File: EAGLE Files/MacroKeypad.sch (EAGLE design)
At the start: 8 parts

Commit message: Clean up old files
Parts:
- removed S2: (no value), switch:255SB
- removed U$6: CHERRY-MX, cherrymx:CHERRY-MX
- added S1: MOMENTARY-SWITCH-SPST-PTH-6.0MM, SparkFun-Switches:MOMENTARY-SWITCH-SPST-PTH-6.0MM
- added U$7: CHERRY-MX-LED, cherrymx:CHERRY-MX-LED
- U$1, U$2, U$3, U$4, U$5: value CHERRY-MX -> CHERRY-MX-LED; device cherrymx:CHERRY-MX -> cherrymx:CHERRY-MX-LED
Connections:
- new net LED+: B1.A3, B1.VCC, U$1.LED+, U$2.LED+, U$3.LED+, U$4.LED+, U$5.LED+, U$7.LED+
- net GND: now also S1.1, U$1.LED-, U$1.SW2, U$2.LED-, U$2.SW2, U$3.LED-, U$3.SW2, U$4.LED-, U$4.SW2, U$5.LED-, U$5.SW2, U$7.LED-, U$7.SW2; no longer S2.O, U$1.PIN-2, U$2.PIN-2, U$3.PIN-2, U$4.PIN-2, U$5.PIN-2, U$6.PIN-2
- net RESET: now also S1.2; no longer S2.P
- net SW1: now also U$7.SW1; no longer U$1.PIN-1
- net SW2: now also U$3.SW1; no longer U$2.PIN-1
- net SW3: now also U$4.SW1; no longer U$3.PIN-1
- net SW4: now also U$1.SW1; no longer U$4.PIN-1
- net SW5: now also U$2.SW1; no longer U$5.PIN-1
- net SW6: now also U$5.SW1; no longer U$6.PIN-1

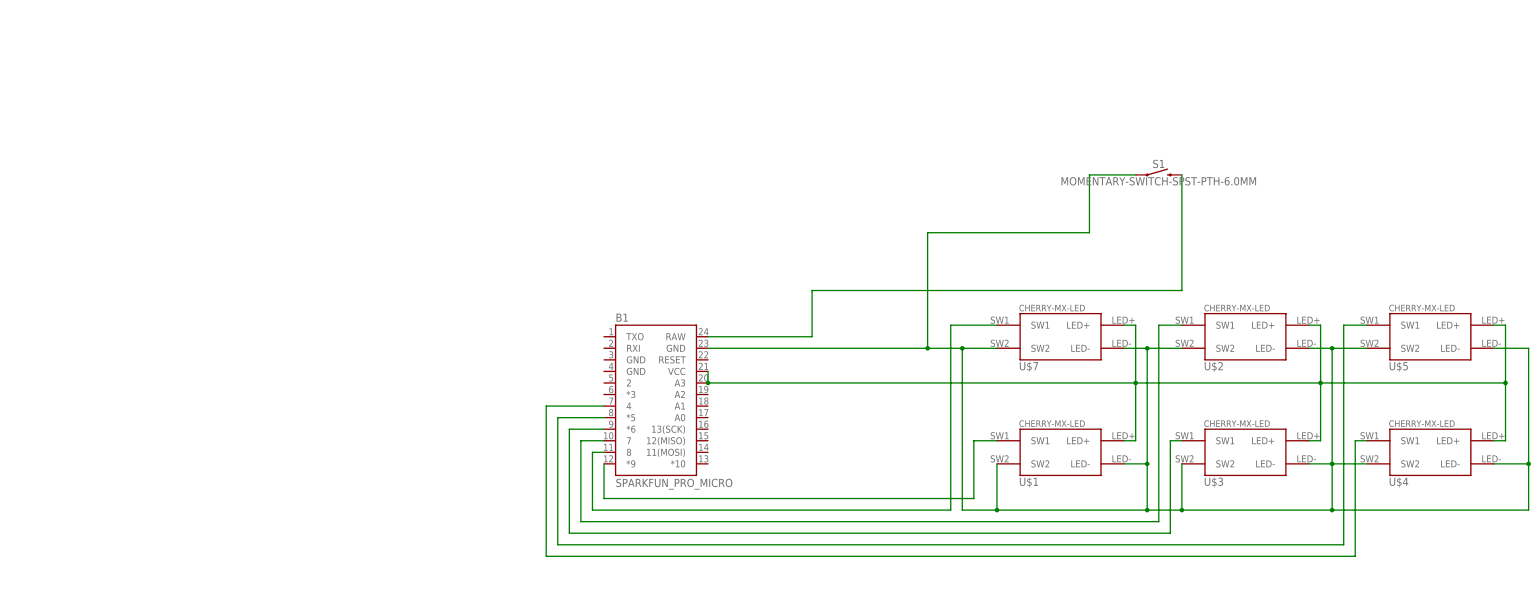
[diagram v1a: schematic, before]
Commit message: Brand new PCB started
Started redesigning PCB and added BOM
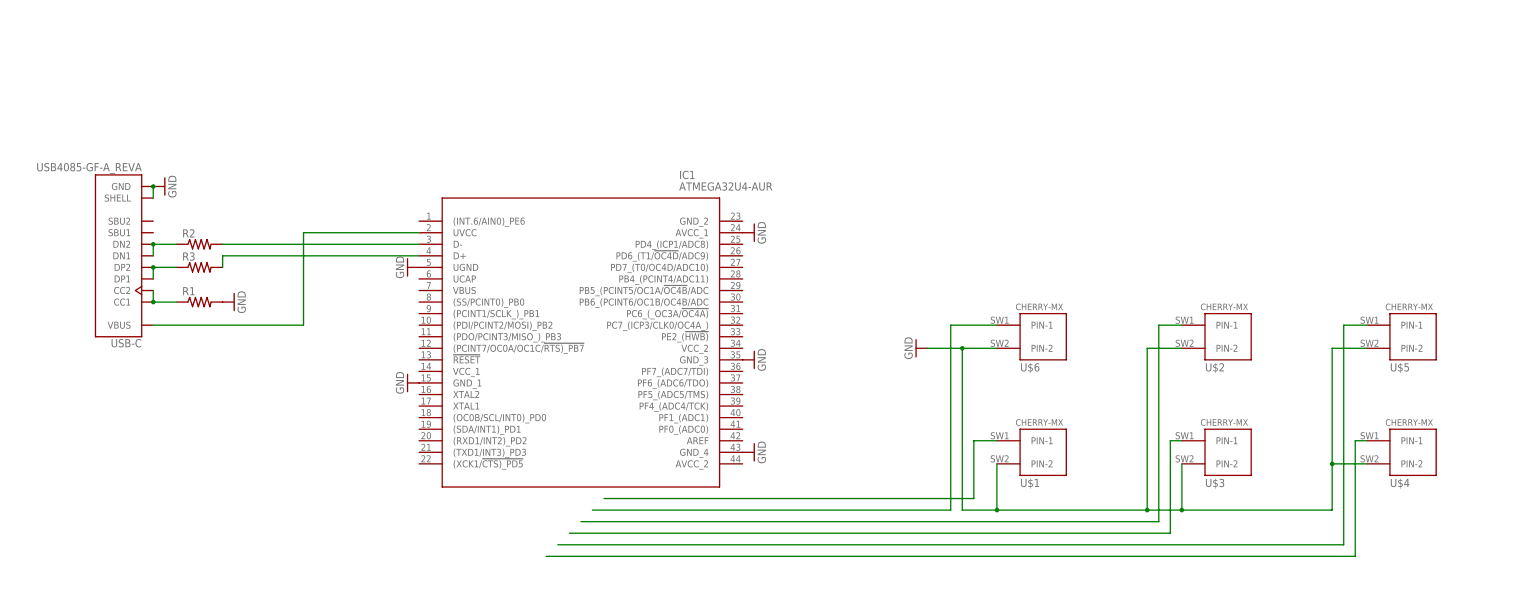
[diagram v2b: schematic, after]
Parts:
- removed B1: SPARKFUN_PRO_MICRO, SparkFun-Boards:SPARKFUN_PRO_MICRO
- removed S1: MOMENTARY-SWITCH-SPST-PTH-6.0MM, SparkFun-Switches:MOMENTARY-SWITCH-SPST-PTH-6.0MM
- removed U$7: CHERRY-MX-LED, cherrymx:CHERRY-MX-LED
- added IC1: ATMEGA32U4-AUR, SamacSys_Parts:ATMEGA32U4-AUR
- added R1: (no value), adafruit:R-US_R0603
- added R2, R3: (no value), adafruit:R-US_R0805
- added U$6: CHERRY-MX, cherrymx:CHERRY-MX
- added USB-C: USB4085-GF-A_REVA, USB4085-GF-A_REVA:USB4085-GF-A_REVA
- U$1, U$2, U$3, U$4, U$5: value CHERRY-MX-LED -> CHERRY-MX; device cherrymx:CHERRY-MX-LED -> cherrymx:CHERRY-MX
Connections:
- removed net LED+: B1.A3, B1.VCC, U$1.LED+, U$2.LED+, U$3.LED+, U$4.LED+, U$5.LED+, U$7.LED+
- removed net RESET: B1.RAW, S1.2
- new net N$1: R1.1, USB-C.CC1, USB-C.CC2
- new net N$2: IC1.UVCC, USB-C.VBUS
- new net N$3: R3.1, USB-C.DP1, USB-C.DP2
- new net N$4: R2.1, USB-C.DN1, USB-C.DN2
- new net N$5: IC1.D-, R2.2
- new net N$6: IC1.D+, R3.2
- net GND: now also IC1.AVCC_1, IC1.GND_1, IC1.GND_3, IC1.GND_4, IC1.UGND, R1.2, U$1.PIN-2, U$2.PIN-2, U$3.PIN-2, U$4.PIN-2, U$5.PIN-2, U$6.PIN-2, USB-C.GND, USB-C.SHELL; no longer B1.GND@2, S1.1, U$1.LED-, U$1.SW2, U$2.LED-, U$2.SW2, U$3.LED-, U$3.SW2, U$4.LED-, U$4.SW2, U$5.LED-, U$5.SW2, U$7.LED-, U$7.SW2
- net SW1: now also U$6.PIN-1; no longer B1.8, U$7.SW1
- net SW2: now also U$3.PIN-1; no longer B1.*6, U$3.SW1
- net SW3: now also U$4.PIN-1; no longer B1.4, U$4.SW1
- net SW4: now also U$1.PIN-1; no longer B1.*9, U$1.SW1
- net SW5: now also U$2.PIN-1; no longer B1.7, U$2.SW1
- net SW6: now also U$5.PIN-1; no longer B1.*5, U$5.SW1

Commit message: Update more files
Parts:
- removed IC1: ATMEGA32U4-AUR, SamacSys_Parts:ATMEGA32U4-AUR
- removed U$1, U$2, U$3, U$4, U$5: CHERRY-MX, cherrymx:CHERRY-MX
- added C1: 1uF, adafruit:C-USC0805
- added IC2: ATMEGA32U4-MU, SamacSys_Parts:ATMEGA32U4-MU
- added SW2, SW3, SW4, SW5, SW6: CHERRY-MX, cherrymx:CHERRY-MX
- R1: value (none) -> 5.1k
- R2, R3: value (none) -> 22Ω
- renumbered U$6 to SW1
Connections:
- net N$1 renamed CC
- removed net SW1: SW1.PIN-1
- removed net SW2: U$3.PIN-1
- removed net SW3: U$4.PIN-1
- removed net SW4: U$1.PIN-1
- removed net SW5: U$2.PIN-1
- removed net SW6: U$5.PIN-1
- new net D+: R2.1, USB-C.DP1, USB-C.DP2
- new net D+RES: IC2.D+, R2.2
- new net D-: R3.1, USB-C.DN1, USB-C.DN2
- new net D-RES: IC2.D-, R3.2
- new net N$1: IC2.(SDA/INT1)_PD1, SW1.PIN-1
- new net UCAP: C1.1, IC2.UCAP
- new net VCC: IC2.AVCC_1, IC2.AVCC_2, IC2.VCC_1
- new net VIN: IC2.UVCC, USB-C.VBUS
- net GND: now also C1.2, IC2.GND_1, IC2.GND_2, IC2.GND_3, IC2.GND_4, IC2.UGND, SW2.PIN-2, SW3.PIN-2, SW4.PIN-2, SW5.PIN-2, SW6.PIN-2; no longer IC1.AVCC_1, IC1.GND_1, IC1.GND_3, IC1.GND_4, IC1.UGND, U$1.PIN-2, U$2.PIN-2, U$3.PIN-2, U$4.PIN-2, U$5.PIN-2
- net N$2: now also IC2.(RXD1/INT2)_PD2, SW2.PIN-1; no longer IC1.UVCC, USB-C.VBUS
- net N$3: now also IC2.(TXD1/INT3)_PD3, SW3.PIN-1; no longer R3.1, USB-C.DP1, USB-C.DP2
- net N$4: now also IC2.PD4_(ICP1/ADC8), SW4.PIN-1; no longer R2.1, USB-C.DN1, USB-C.DN2
- net N$5: now also IC2.(XCK1/!CTS)_PD5, SW5.PIN-1; no longer IC1.D-, R2.2
- net N$6: now also IC2.PD6_(T1/!OC4D!/ADC9), SW6.PIN-1; no longer IC1.D+, R3.2
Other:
- moved on the sheet: R2, R3

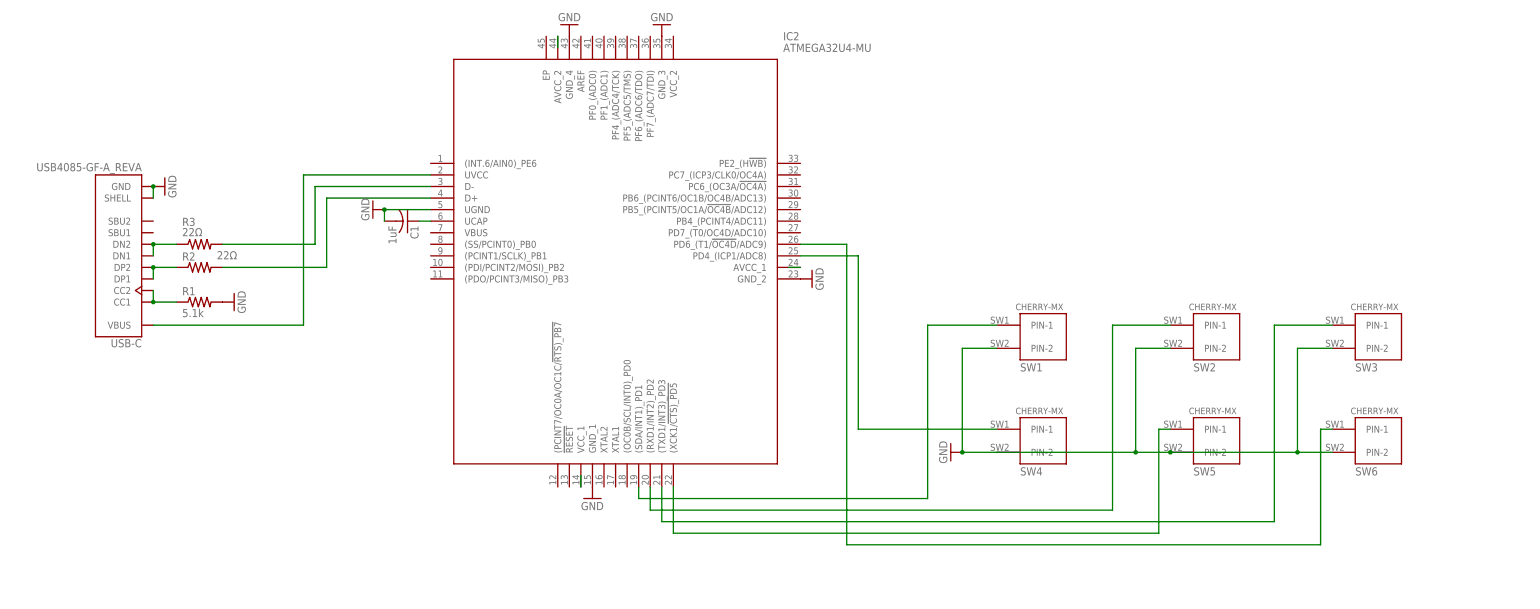
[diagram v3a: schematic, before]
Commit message: (Almost) Finished with the redo
Pretty much done, just need to fix USB-C port footprint and make code for the new board
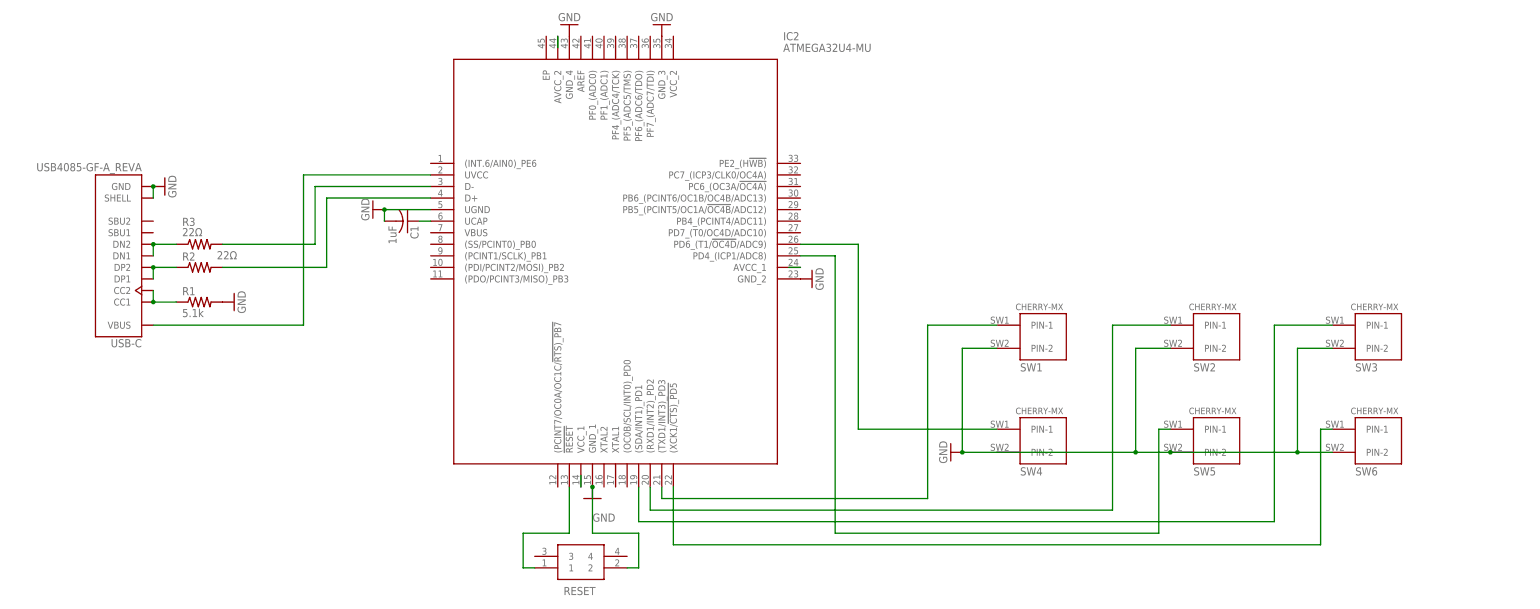
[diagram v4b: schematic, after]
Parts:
- added RESET: LL3303F065QG, SamacSys_Parts:LL3303F065QG
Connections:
- net N$2 renamed SW2
- removed net N$1: IC2.(SDA/INT1)_PD1, SW1.PIN-1
- removed net N$3: IC2.(TXD1/INT3)_PD3, SW3.PIN-1
- removed net N$4: IC2.PD4_(ICP1/ADC8), SW4.PIN-1
- removed net N$5: IC2.(XCK1/!CTS)_PD5, SW5.PIN-1
- removed net N$6: IC2.PD6_(T1/!OC4D!/ADC9), SW6.PIN-1
- new net RESET: IC2.!RESET, RESET.1
- new net SW1: IC2.(TXD1/INT3)_PD3, SW1.PIN-1
- new net SW3: IC2.(SDA/INT1)_PD1, SW3.PIN-1
- new net SW4: IC2.PD6_(T1/!OC4D!/ADC9), SW4.PIN-1
- new net SW5: IC2.PD4_(ICP1/ADC8), SW5.PIN-1
- new net SW6: IC2.(XCK1/!CTS)_PD5, SW6.PIN-1
- net GND: now also RESET.2
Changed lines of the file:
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@@
 <part name="GND6" library="supply1" library_urn="urn:adsk.eagle:library:371" deviceset="GND" device=""/>
 <part name="GND7" library="supply1" library_urn="urn:adsk.eagle:library:371" deviceset="GND" device=""/>
+<part name="RESET" library="SamacSys_Parts" deviceset="LL3303F065QG" device=""/>
 </parts>
 <sheets>
@@
 </instance>
 <instance part="GND4" gate="1" x="-93.98" y="45.72" smashed="yes">
-<attribute name="VALUE" x="-96.52" y="43.18" size="1.778" layer="96"/>
+<attribute name="VALUE" x="-93.98" y="40.64" size="1.778" layer="96"/>
 </instance>
 <instance part="GND5" gate="1" x="-45.72" y="93.98" smashed="yes" rot="R90">
@@
 <instance part="GND7" gate="1" x="-78.74" y="149.86" smashed="yes" rot="R180">
 <attribute name="VALUE" x="-76.2" y="152.4" size="1.778" layer="96" rot="R180"/>
+</instance>
+<instance part="RESET" gate="G$1" x="-106.68" y="33.02" smashed="yes">
+<attribute name="NAME" x="-100.33" y="25.4" size="1.778" layer="95" align="center-left"/>
 </instance>
 </instances>
@@
 <pinref part="IC2" gate="G$1" pin="GND_1"/>
 <pinref part="GND4" gate="1" pin="GND"/>
+<pinref part="RESET" gate="G$1" pin="2"/>
+<wire x1="-86.36" y1="30.48" x2="-83.82" y2="30.48" width="0.1524" layer="91"/>
+<wire x1="-83.82" y1="30.48" x2="-83.82" y2="38.1" width="0.1524" layer="91"/>
+<wire x1="-83.82" y1="38.1" x2="-93.98" y2="38.1" width="0.1524" layer="91"/>
+<wire x1="-93.98" y1="38.1" x2="-93.98" y2="48.26" width="0.1524" layer="91"/>
+<junction x="-93.98" y="48.26"/>
 </segment>
 <segment>
@@
 </segment>
 </net>
-<net name="N$1" class="0">
+<net name="SW1" class="0">
 <segment>
 <pinref part="SW1" gate="G$1" pin="PIN-1"/>
 <wire x1="-5.08" y1="83.82" x2="-20.32" y2="83.82" width="0.1524" layer="91"/>
 <wire x1="-20.32" y1="83.82" x2="-20.32" y2="45.72" width="0.1524" layer="91"/>
-<pinref part="IC2" gate="G$1" pin="(SDA/INT1)_PD1"/>
-<wire x1="-20.32" y1="45.72" x2="-83.82" y2="45.72" width="0.1524" layer="91"/>
-<wire x1="-83.82" y1="45.72" x2="-83.82" y2="48.26" width="0.1524" layer="91"/>
-</segment>
-</net>
-<net name="N$2" class="0">
+<wire x1="-20.32" y1="45.72" x2="-78.74" y2="45.72" width="0.1524" layer="91"/>
+<pinref part="IC2" gate="G$1" pin="(TXD1/INT3)_PD3"/>
+<wire x1="-78.74" y1="45.72" x2="-78.74" y2="48.26" width="0.1524" layer="91"/>
+</segment>
+</net>
+<net name="SW2" class="0">
 <segment>
 <pinref part="SW2" gate="G$1" pin="PIN-1"/>
@@
 </segment>
 </net>
-<net name="N$3" class="0">
+<net name="SW3" class="0">
 <segment>
 <pinref part="SW3" gate="G$1" pin="PIN-1"/>
 <wire x1="68.58" y1="83.82" x2="55.88" y2="83.82" width="0.1524" layer="91"/>
 <wire x1="55.88" y1="83.82" x2="55.88" y2="40.64" width="0.1524" layer="91"/>
-<pinref part="IC2" gate="G$1" pin="(TXD1/INT3)_PD3"/>
-<wire x1="55.88" y1="40.64" x2="-78.74" y2="40.64" width="0.1524" layer="91"/>
-<wire x1="-78.74" y1="40.64" x2="-78.74" y2="48.26" width="0.1524" layer="91"/>
-</segment>
-</net>
-<net name="N$4" class="0">
+<wire x1="55.88" y1="40.64" x2="-83.82" y2="40.64" width="0.1524" layer="91"/>
+<pinref part="IC2" gate="G$1" pin="(SDA/INT1)_PD1"/>
+<wire x1="-83.82" y1="48.26" x2="-83.82" y2="40.64" width="0.1524" layer="91"/>
+</segment>
+</net>
+<net name="SW4" class="0">
 <segment>
 <pinref part="SW4" gate="G$1" pin="PIN-1"/>
 <wire x1="-5.08" y1="60.96" x2="-35.56" y2="60.96" width="0.1524" layer="91"/>
-<wire x1="-35.56" y1="60.96" x2="-35.56" y2="99.06" width="0.1524" layer="91"/>
-<pinref part="IC2" gate="G$1" pin="PD4_(ICP1/ADC8)"/>
-<wire x1="-35.56" y1="99.06" x2="-48.26" y2="99.06" width="0.1524" layer="91"/>
-</segment>
-</net>
-<net name="N$5" class="0">
+<wire x1="-35.56" y1="60.96" x2="-35.56" y2="101.6" width="0.1524" layer="91"/>
+<pinref part="IC2" gate="G$1" pin="PD6_(T1/!OC4D!/ADC9)"/>
+<wire x1="-35.56" y1="101.6" x2="-48.26" y2="101.6" width="0.1524" layer="91"/>
+</segment>
+</net>
+<net name="SW5" class="0">
 <segment>
 <pinref part="SW5" gate="G$1" pin="PIN-1"/>
 <wire x1="33.02" y1="60.96" x2="30.48" y2="60.96" width="0.1524" layer="91"/>
 <wire x1="30.48" y1="60.96" x2="30.48" y2="38.1" width="0.1524" layer="91"/>
-<pinref part="IC2" gate="G$1" pin="(XCK1/!CTS)_PD5"/>
-<wire x1="30.48" y1="38.1" x2="-76.2" y2="38.1" width="0.1524" layer="91"/>
-<wire x1="-76.2" y1="38.1" x2="-76.2" y2="48.26" width="0.1524" layer="91"/>
-</segment>
-</net>
-<net name="N$6" class="0">
+<wire x1="30.48" y1="38.1" x2="-40.64" y2="38.1" width="0.1524" layer="91"/>
+<pinref part="IC2" gate="G$1" pin="PD4_(ICP1/ADC8)"/>
+<wire x1="-48.26" y1="99.06" x2="-40.64" y2="99.06" width="0.1524" layer="91"/>
+<wire x1="-40.64" y1="99.06" x2="-40.64" y2="38.1" width="0.1524" layer="91"/>
+</segment>
+</net>
+<net name="SW6" class="0">
 <segment>
 <pinref part="SW6" gate="G$1" pin="PIN-1"/>
 <wire x1="68.58" y1="60.96" x2="66.04" y2="60.96" width="0.1524" layer="91"/>
 <wire x1="66.04" y1="60.96" x2="66.04" y2="35.56" width="0.1524" layer="91"/>
-<wire x1="66.04" y1="35.56" x2="-38.1" y2="35.56" width="0.1524" layer="91"/>
-<wire x1="-38.1" y1="35.56" x2="-38.1" y2="101.6" width="0.1524" layer="91"/>
-<pinref part="IC2" gate="G$1" pin="PD6_(T1/!OC4D!/ADC9)"/>
-<wire x1="-38.1" y1="101.6" x2="-48.26" y2="101.6" width="0.1524" layer="91"/>
-</segment>
-</net>
+<wire x1="66.04" y1="35.56" x2="-76.2" y2="35.56" width="0.1524" layer="91"/>
+<pinref part="IC2" gate="G$1" pin="(XCK1/!CTS)_PD5"/>
+<wire x1="-76.2" y1="35.56" x2="-76.2" y2="48.26" width="0.1524" layer="91"/>
+</segment>
+</net>
+<net name="RESET" class="0">
+<segment>
+<pinref part="IC2" gate="G$1" pin="!RESET"/>
+<wire x1="-99.06" y1="48.26" x2="-99.06" y2="38.1" width="0.1524" layer="91"/>
+<wire x1="-99.06" y1="38.1" x2="-109.22" y2="38.1" width="0.1524" layer="91"/>
+<pinref part="RESET" gate="G$1" pin="1"/>
+<wire x1="-109.22" y1="38.1" x2="-109.22" y2="30.48" width="0.1524" layer="91"/>
+<wire x1="-109.22" y1="30.48" x2="-106.68" y2="30.48" width="0.1524" layer="91"/>
+</segment>
+</net>
